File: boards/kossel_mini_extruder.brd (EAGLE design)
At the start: 66.9 x 57.9 mm, 33 parts

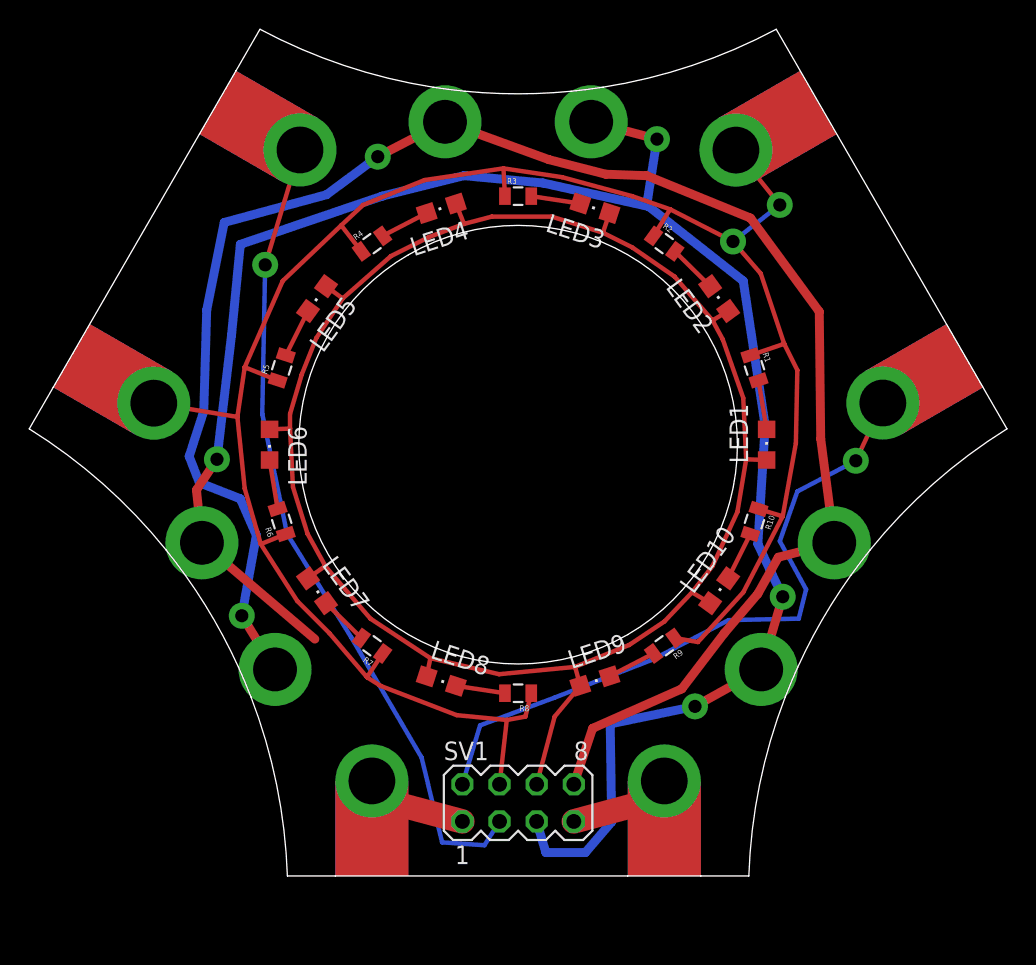
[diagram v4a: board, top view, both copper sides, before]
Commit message: put fan and hot back on same 12v to make space to breakout thermister gnd
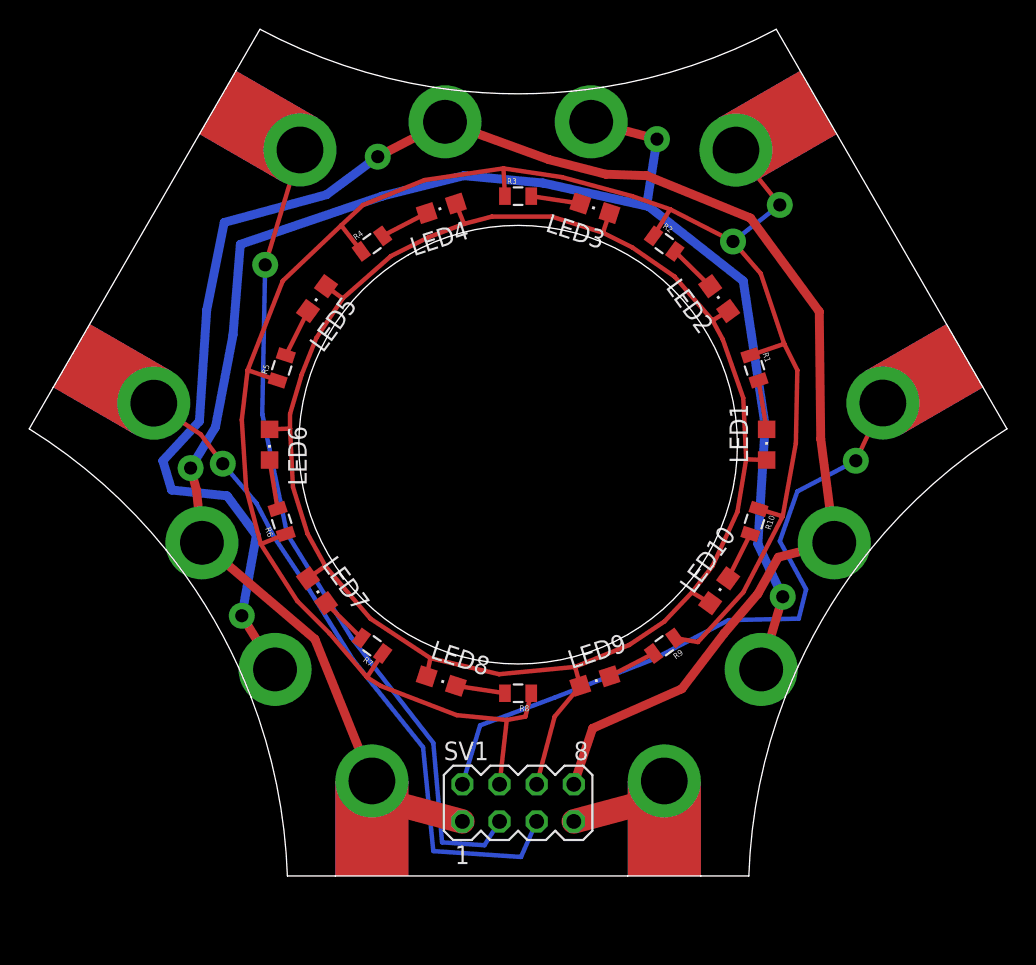
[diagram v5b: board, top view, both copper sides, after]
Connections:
- net FAN_VCC renamed VCC
- removed net FAN_12V: FAN_0_12V.P$1, FAN_1_12V.P$1, FAN_2_12V.P$1, SV1.5
- removed net HOT_12V: HOT_12V.P$1, HOT_12V.P$2, HOT_12V.P$3, SV1.1
- new net 12V: FAN_0_12V.P$1, FAN_1_12V.P$1, FAN_2_12V.P$1, HOT_12V.P$1, HOT_12V.P$2, HOT_12V.P$3, SV1.1
- new net N$8: SV1.5, THERM_GND.P$1, THERM_GND.P$2, THERM_GND.P$3
- net GND: no longer THERM_GND.P$1, THERM_GND.P$2, THERM_GND.P$3
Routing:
- net FAN_12V: track 130.4 -> 0.00 mm, vias 4 -> 0
- net 12V: track 0.00 -> 125.7 mm, vias 0 -> 3
- net N$8: track 0.00 -> 49.2 mm, vias 0 -> 1
- net HOT_12V: track 10.2 -> 0.00 mm
- net GND: track 152.1 -> 142.6 mm
- net N$17: track 122.4 -> 125.1 mm

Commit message: removed fan stuff and added red leds
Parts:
- removed FAN_0_12V, FAN_0_PWM, FAN_1_12V, FAN_1_PWM, FAN_2_12V, FAN_2_PWM: LUG2.3, OBKP_Effector_PCB:2.3MM
- removed LED7: (no value), SparkFun-LED:CHIPLED_0805
- removed R7: (no value), SparkFun-Passives:0805
- added LED11, LED12, LED13: (no value), SparkFun-LED:CHIPLED_0805
- added R11, R12, R13: (no value), SparkFun-Passives:0805
- moved R8 10.1 mm to (22.9, 12.6), turned to 60 degrees
- moved R9 8.11 mm to (36.7, 10.1), turned to 126 degrees
- moved R10 7.77 mm to (47.6, 16.1), turned to 147 degrees
- moved R1 7.03 mm to (52.1, 27.9), turned to 198 degrees
- moved LED8 6.17 mm to (22.2, 15.6), turned to 230 degrees
- moved R3 5.26 mm to (37.9, 47.9), turned to 255 degrees
- moved LED9 5.12 mm to (33.3, 11.7), turned to 270 degrees
- moved R2 4.46 mm to (47.4, 42.1), turned to 234 degrees
- moved R4 3.86 mm to (24.4, 46.4), turned to 306 degrees
- moved LED10 3.84 mm to (44.4, 16.0), turned to 310 degrees
- moved R5 3.48 mm to (15.7, 37.6), turned to 342 degrees
- moved LED1 3.21 mm to (49.8, 25.8), turned to 350 degrees
- moved LED6 3.01 mm to (16.2, 26.0), turned to 190 degrees
- moved R6 2.31 mm to (14.6, 23.0), turned to 18 degrees
- moved LED2 2.08 mm to (48.0, 37.3), turned to 30 degrees
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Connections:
- removed net 12V: FAN_0_12V.P$1, FAN_1_12V.P$1, FAN_2_12V.P$1, HOT_12V.P$1, HOT_12V.P$2, HOT_12V.P$3, SV1.1
- removed net N$7: LED7.C, R7.2
- new net N$10: HOT_12V.P$1, HOT_12V.P$2, HOT_12V.P$3, SV1.1
- new net N$16: LED11.C, R11.2
- new net N$18: LED13.C, R13.2
- new net VCC1: LED11.A, LED12.A, LED13.A, SV1.8
- net GND: now also R11.1, R12.1, R13.1; no longer PROBE_GND.P$1, PROBE_GND.P$2, PROBE_GND.P$3, R7.1
- net N$17: now also LED12.C, R12.2; no longer FAN_0_PWM.P$1, FAN_1_PWM.P$1, FAN_2_PWM.P$1, SV1.8
- net N$8: now also PROBE_GND.P$1, PROBE_GND.P$2, PROBE_GND.P$3
- net VCC: no longer LED7.A
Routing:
- net 12V: track 125.7 -> 0.00 mm, vias 3 -> 0
- net VCC1: track 0.00 -> 125.3 mm
- net N$17: track 125.1 -> 0.00 mm, vias 2 -> 0
- net N$8: track 49.2 -> 110.6 mm, vias 1 -> 2
- net GND: track 142.6 -> 122.7 mm, vias 2 -> 0
- net VCC: track 119.7 -> 110.2 mm
- net N$10: track 0.00 -> 9.46 mm
- net N$7: track 3.39 -> 0.00 mm
- net N$20: track 49.1 -> 46.3 mm
- net N$11: track 59.2 -> 61.4 mm
- net N$5: track 3.39 -> 1.95 mm
- net N$1: track 3.39 -> 1.99 mm
- net N$4: track 3.39 -> 2.15 mm
- net N$14: track 3.39 -> 2.29 mm
- net N$9: track 3.39 -> 2.29 mm
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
